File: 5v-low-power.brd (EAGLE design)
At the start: 68.6 x 40.3 mm, 37 parts, among them J1 Bypass, J2 En, J3 12v, J4 5V Out, J5 LED EN, J6 POWERPOLE_POWER25A, J7 POWERPOLE_POWER25A, Q1 SI4532ADY, U1 LT1934ES6TRMPBF

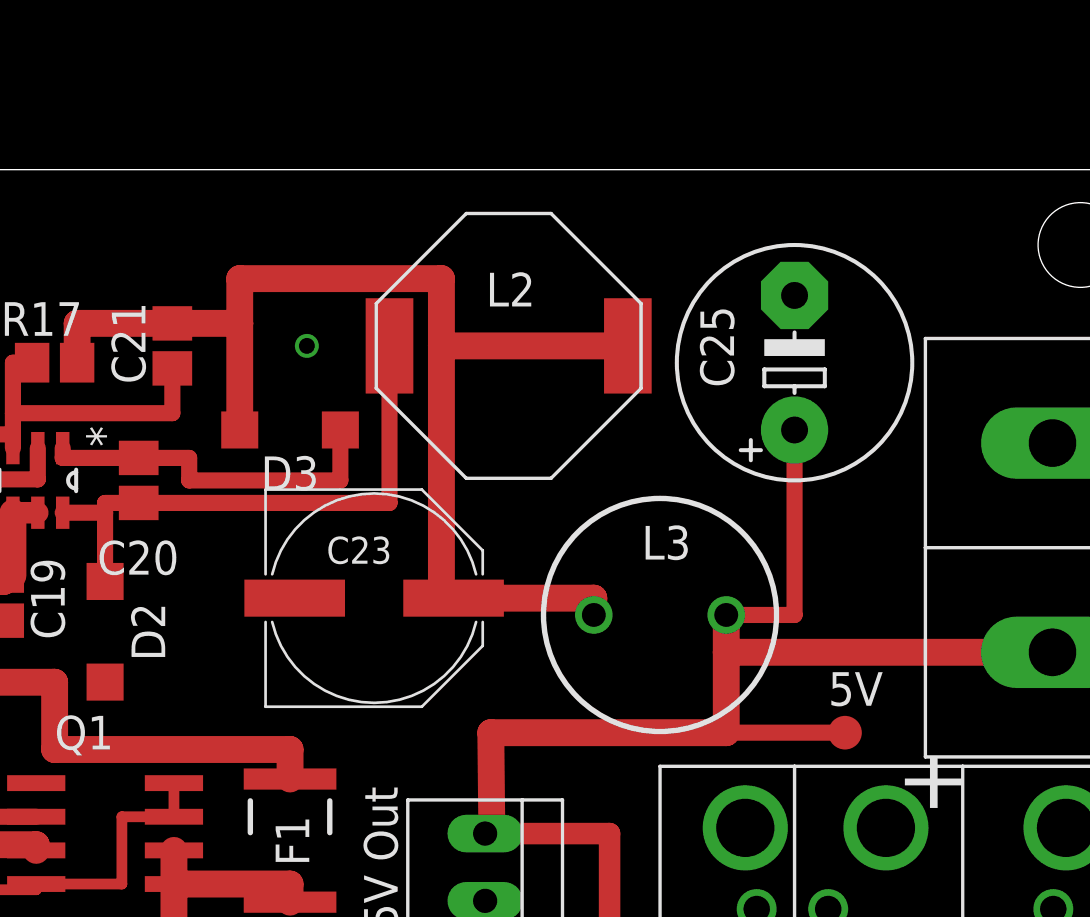
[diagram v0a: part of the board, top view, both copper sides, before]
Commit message: now uses DR127 footprint for big inductor
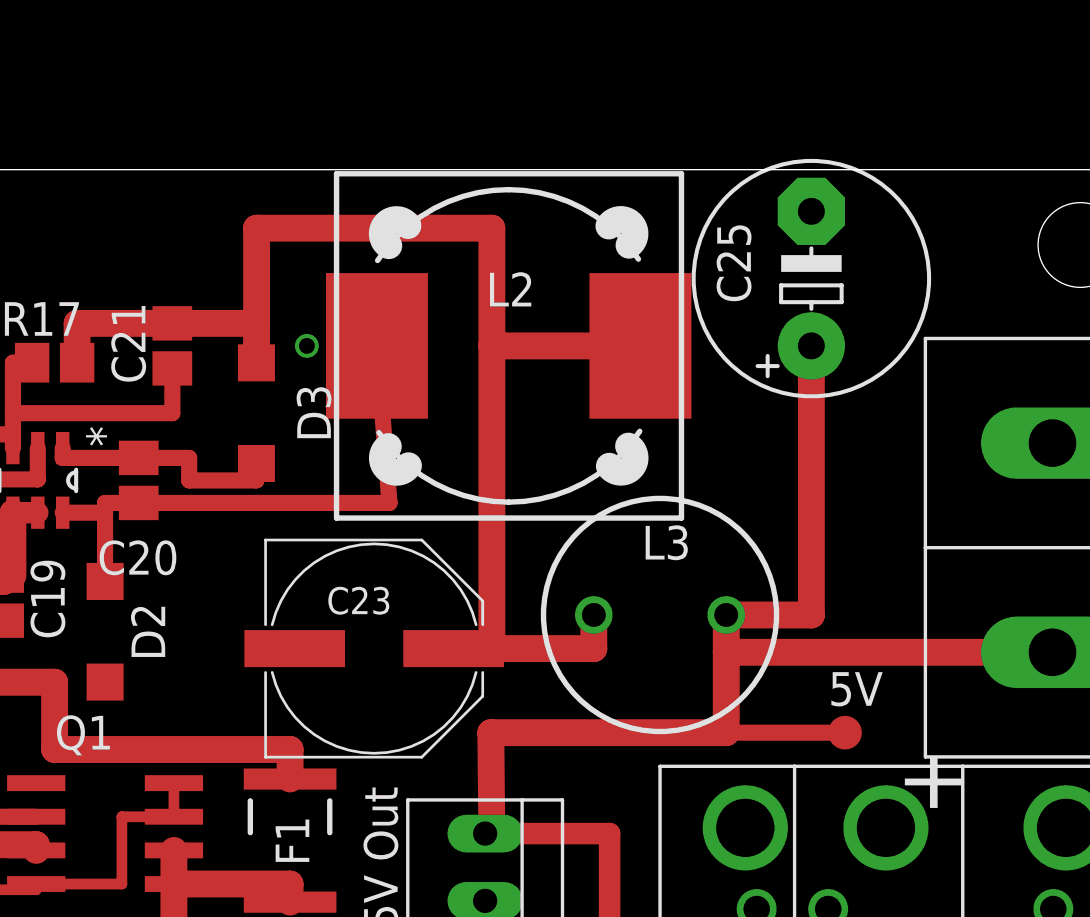
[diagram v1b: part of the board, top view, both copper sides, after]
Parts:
- L2: device farnell-parts:1048 -> inductors:DR127
- moved C25 3.24 mm to (54.6, 36.2)
- moved C23 1.90 mm to (38.1, 22.2)
- moved D3 1.42 mm to (33.7, 31.1), turned to 90 degrees
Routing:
- net N$117: track 13.6 -> 9.17 mm
- net N$107: track 46.5 -> 50.3 mm
- net 5V: track 76.2 -> 80.0 mm
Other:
- board text added: "V0.3"
- board text removed: "V0.2"
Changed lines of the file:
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@@
 <setting verticaltext="up"/>
 </settings>
-<grid distance="25" unitdist="mil" unit="mm" style="lines" multiple="1" display="yes" altdistance="5" altunitdist="mil" altunit="mm"/>
+<grid distance="25" unitdist="mil" unit="mil" style="lines" multiple="1" display="yes" altdistance="5" altunitdist="mil" altunit="mm"/>
 <layers>
 <layer number="1" name="Top" color="4" fill="1" visible="yes" active="yes"/>
@@
 <hole x="3.175" y="3.175" drill="3.2"/>
 <text x="24.13" y="37.465" size="1.27" layer="51">5V Low Power</text>
-<text x="2.54" y="6.35" size="1.778" layer="51" rot="R90">V0.2</text>
+<text x="2.54" y="6.35" size="1.778" layer="51" rot="R90">V0.3</text>
 <text x="2.54" y="14.605" size="1.778" layer="51" rot="R90">PJB</text>
-<text x="53.975" y="38.1" size="1.778" layer="51">250mA</text>
+<text x="5.715" y="0" size="1.778" layer="51">250mA</text>
 </plain>
 <attributes>
@@
 <attribute name="VALUE" x="31.75" y="35.433" size="1.27" layer="27" rot="R270"/>
 </element>
-<element name="L2" library="farnell-parts" package="1048" value="68uH" x="43.18" y="33.655" smashed="yes">
+<element name="L2" library="inductors" package="DR127" value="68uH" x="43.18" y="33.655" smashed="yes">
 <attribute name="NAME" x="42.32" y="35.145" size="1.27" layer="25" ratio="10"/>
 <attribute name="VALUE" x="41.485" y="31.5" size="1.27" layer="27" ratio="10"/>
 </element>
-<element name="C23" library="rcl" package="PANASONIC_E" value="68uF" x="38.1" y="24.13"/>
-<element name="D3" library="diode" package="SOD123" value="MBR0540" x="34.925" y="30.48" smashed="yes" rot="R180">
-<attribute name="NAME" x="36.025" y="29.48" size="1.27" layer="25" rot="R180"/>
+<element name="C23" library="rcl" package="PANASONIC_E" value="68uF" x="38.1" y="22.225"/>
+<element name="D3" library="diode" package="SOD123" value="MBR0540" x="33.655" y="31.115" smashed="yes" rot="R90">
+<attribute name="NAME" x="36.465" y="30.015" size="1.27" layer="25" rot="R90"/>
 </element>
 <element name="L3" library="rcl" package="6000-XXXX-RC" value="20uH" x="48.895" y="23.495" smashed="yes">
@@
 <attribute name="VALUE" x="46.9294" y="20.2594" size="1.27" layer="27"/>
 </element>
-<element name="C25" library="rcl" package="E5-8,5" value="330uF" x="53.975" y="33.02" smashed="yes" rot="R90">
-<attribute name="NAME" x="51.689" y="32.0802" size="1.27" layer="25" ratio="10" rot="R90"/>
-<attribute name="VALUE" x="56.9976" y="30.5054" size="1.27" layer="27" ratio="10" rot="R90"/>
+<element name="C25" library="rcl" package="E5-8,5" value="330uF" x="54.61" y="36.195" smashed="yes" rot="R90">
+<attribute name="NAME" x="52.324" y="35.2552" size="1.27" layer="25" ratio="10" rot="R90"/>
+<attribute name="VALUE" x="57.6326" y="33.6804" size="1.27" layer="27" ratio="10" rot="R90"/>
 </element>
 <element name="5V" library="testpad" package="B1,27" value="5V B" x="55.88" y="19.05">
@@
 <wire x1="27.94" y1="27.725" x2="27.94" y2="27.3558" width="0.6096" layer="1"/>
 <wire x1="29.21" y1="27.725" x2="38.68" y2="27.725" width="0.6096" layer="1"/>
-<wire x1="38.68" y1="27.725" x2="38.68" y2="33.655" width="0.6096" layer="1"/>
+<wire x1="38.68" y1="27.725" x2="38.205" y2="33.655" width="0.6096" layer="1"/>
 </signal>
 <signal name="N$117">
@@
 <wire x1="29.21" y1="29.425" x2="31.115" y2="29.425" width="0.6096" layer="1"/>
 <wire x1="31.115" y1="29.425" x2="31.115" y2="28.575" width="0.6096" layer="1"/>
-<wire x1="31.115" y1="28.575" x2="36.825" y2="28.575" width="0.6096" layer="1"/>
-<wire x1="36.825" y1="28.575" x2="36.825" y2="30.48" width="0.6096" layer="1"/>
+<wire x1="31.115" y1="28.575" x2="33.65" y2="28.575" width="0.6096" layer="1"/>
+<wire x1="33.65" y1="28.575" x2="33.655" y2="29.215" width="0.6096" layer="1"/>
 </signal>
 <signal name="N$118">
@@
 <wire x1="26.885" y1="33.02" x2="26.885" y2="34.505" width="1.016" layer="1"/>
 <wire x1="26.885" y1="34.505" x2="30.48" y2="34.505" width="1.016" layer="1"/>
-<wire x1="33.025" y1="30.48" x2="33.025" y2="34.505" width="1.016" layer="1"/>
-<wire x1="33.025" y1="34.505" x2="30.48" y2="34.505" width="1.016" layer="1"/>
-<wire x1="41.1" y1="24.13" x2="40.64" y2="24.13" width="0.6096" layer="1"/>
-<wire x1="40.64" y1="24.13" x2="40.64" y2="33.655" width="1.016" layer="1"/>
-<wire x1="40.64" y1="33.655" x2="40.64" y2="36.195" width="1.016" layer="1"/>
-<wire x1="40.64" y1="36.195" x2="33.025" y2="36.195" width="1.016" layer="1"/>
-<wire x1="33.025" y1="36.195" x2="33.025" y2="34.505" width="1.016" layer="1"/>
-<wire x1="47.68" y1="33.655" x2="40.64" y2="33.655" width="1.016" layer="1"/>
-<wire x1="41.1" y1="24.13" x2="46.395" y2="24.13" width="1.016" layer="1"/>
-<wire x1="46.395" y1="24.13" x2="46.395" y2="23.495" width="1.016" layer="1"/>
+<wire x1="33.655" y1="33.015" x2="33.66" y2="34.505" width="1.016" layer="1"/>
+<wire x1="33.66" y1="34.505" x2="30.48" y2="34.505" width="1.016" layer="1"/>
+<wire x1="42.545" y1="22.225" x2="42.545" y2="33.655" width="1.016" layer="1"/>
+<wire x1="42.545" y1="33.655" x2="42.545" y2="38.1" width="1.016" layer="1"/>
+<wire x1="42.545" y1="38.1" x2="33.66" y2="38.1" width="1.016" layer="1"/>
+<wire x1="33.66" y1="38.1" x2="33.66" y2="34.505" width="1.016" layer="1"/>
+<wire x1="48.155" y1="33.655" x2="42.545" y2="33.655" width="1.016" layer="1"/>
+<wire x1="41.1" y1="22.225" x2="42.545" y2="22.225" width="1.016" layer="1"/>
+<wire x1="42.545" y1="22.225" x2="46.395" y2="22.225" width="1.016" layer="1"/>
+<wire x1="46.395" y1="22.225" x2="46.395" y2="23.495" width="1.016" layer="1"/>
 </signal>
 <signal name="VCC_HP2_SW">
@@
 <contactref element="J4" pad="2"/>
 <contactref element="J6" pad="RED"/>
-<wire x1="51.395" y1="23.495" x2="53.975" y2="23.495" width="0.6096" layer="1"/>
-<wire x1="53.975" y1="23.495" x2="53.975" y2="29.935" width="0.6096" layer="1"/>
-<wire x1="53.975" y1="29.935" x2="53.975" y2="30.48" width="1.016" layer="1"/>
+<wire x1="51.395" y1="23.495" x2="54.61" y2="23.495" width="1.016" layer="1"/>
+<wire x1="54.61" y1="23.495" x2="54.61" y2="33.655" width="1.016" layer="1"/>
 <wire x1="42.291" y1="15.24" x2="42.545" y2="15.24" width="1.016" layer="1"/>
 <wire x1="42.545" y1="15.24" x2="42.505" y2="19.05" width="1.016" layer="1"/>
